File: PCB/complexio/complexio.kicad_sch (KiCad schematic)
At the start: 22 parts, among them J2 Conn_01x21_Pin, J3 USB_C_Receptacle_USB2.0_16P, SW1 SW_SPDT, U2 TB6612FNG, U21 AT24CM01, U22 STM32F303RBT6, U3 TB6612FNG

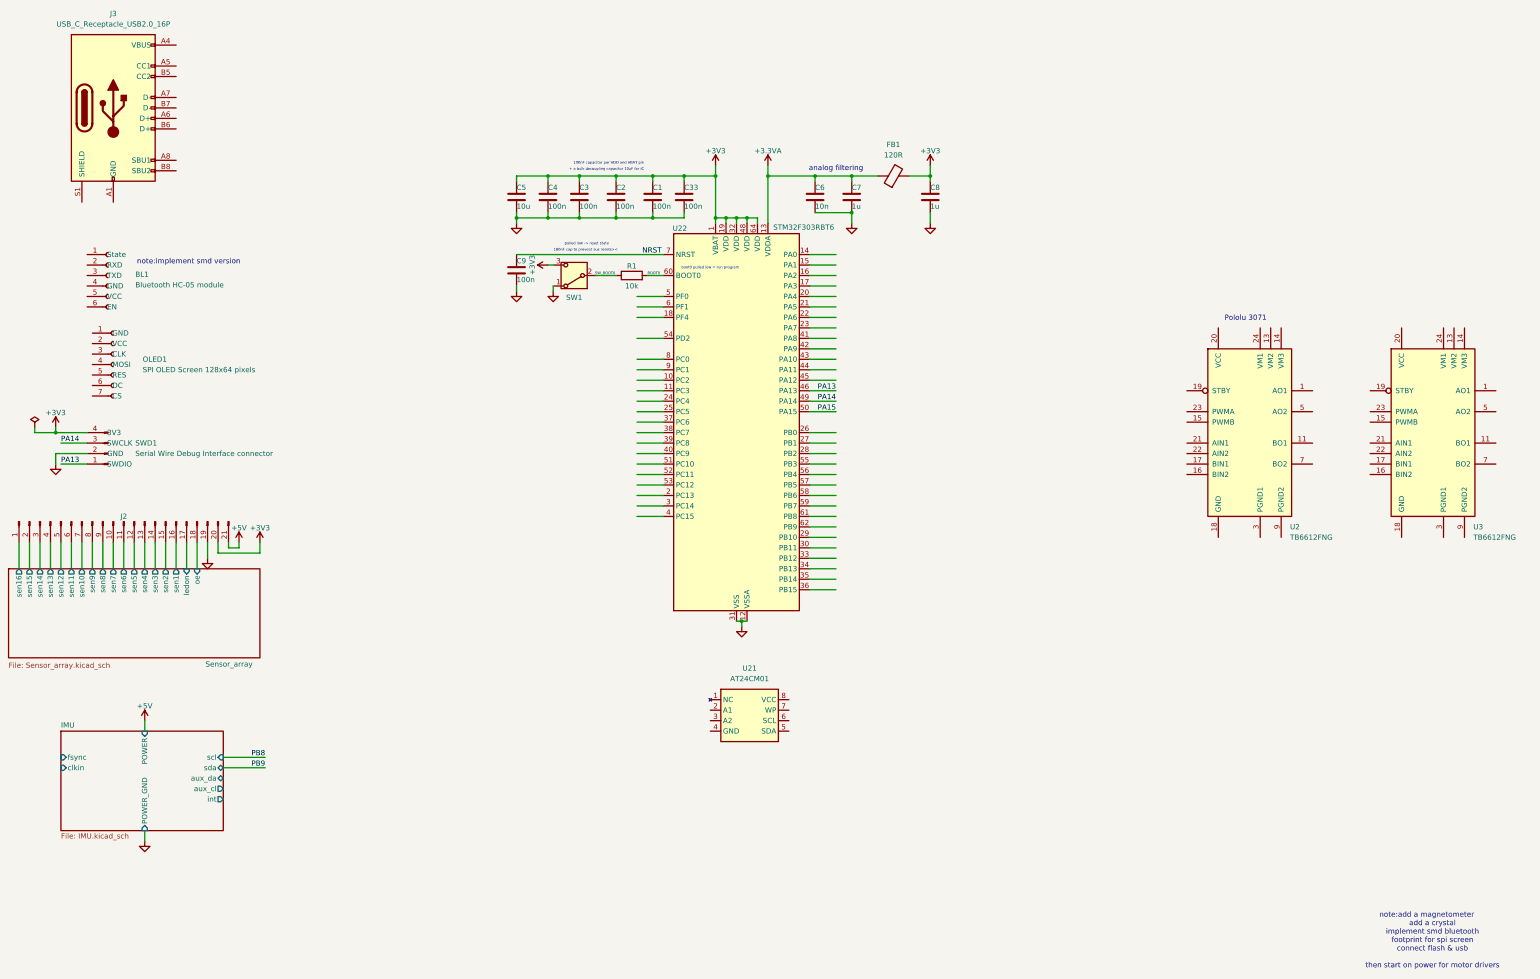
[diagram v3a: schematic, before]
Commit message: Advanced with schem & resolved main power problem
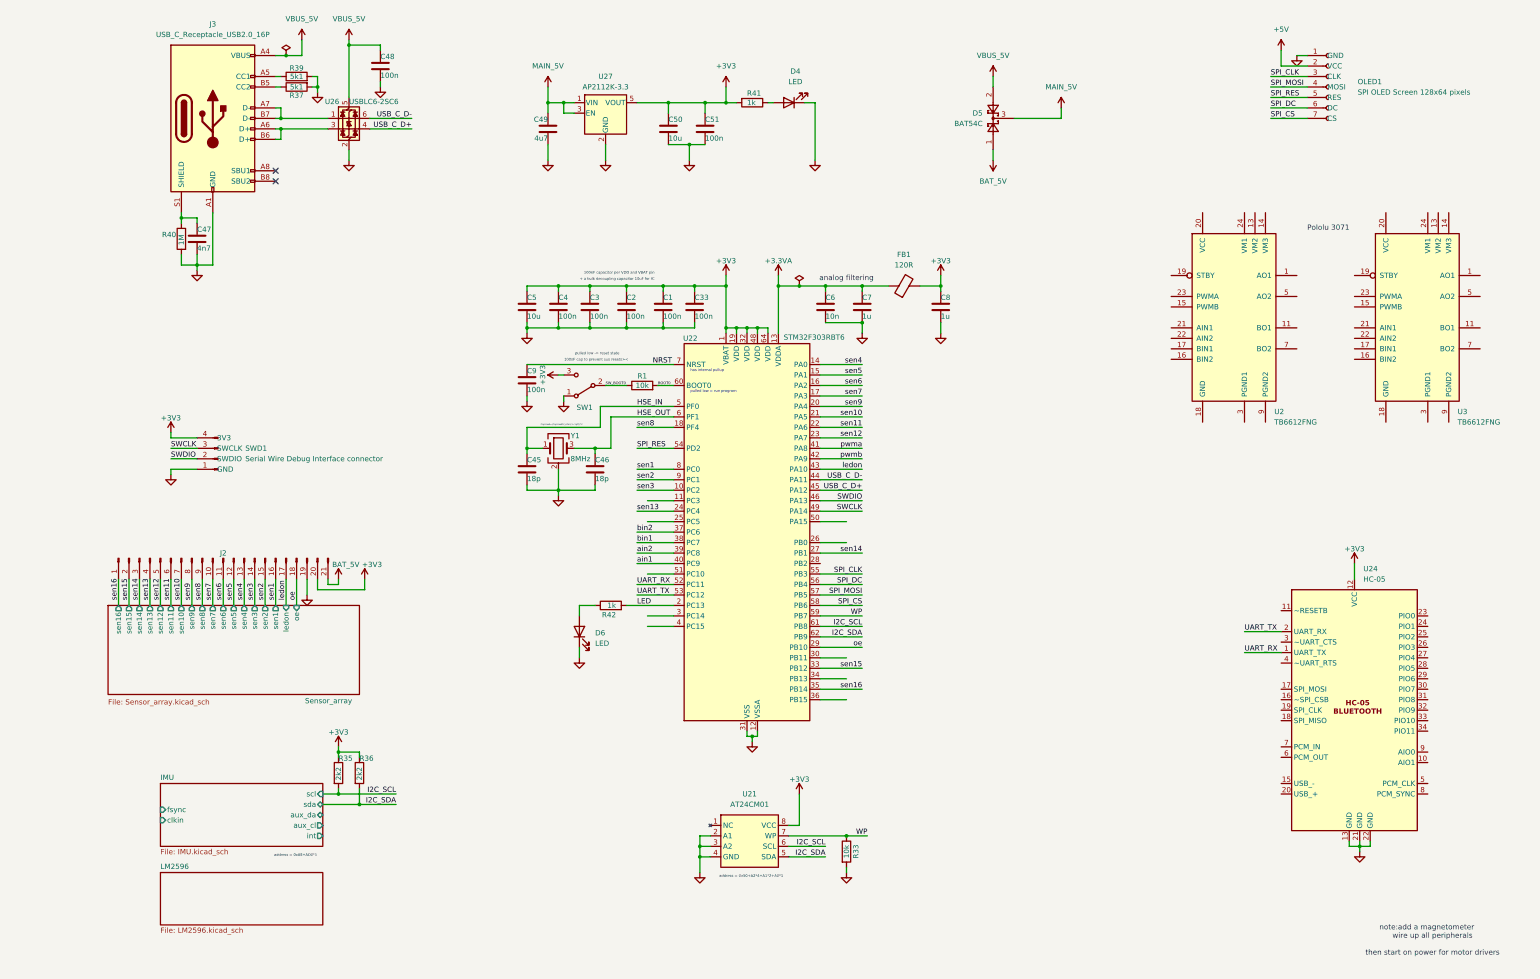
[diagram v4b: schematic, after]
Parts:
- removed BL1: Bluetooth HC-05 module, Connector_PinSocket_2.54mm:PinSocket_1x07_P2.54mm_Horizontal, symbol Connector:Conn_01x06_Socket
- added C45, C46: 18p, Capacitor_SMD:C_0402_1005Metric, symbol Device:C
- added C47: 4n7, Capacitor_SMD:C_1206_3216Metric, symbol Device:C
- added C48, C51: 100n, Capacitor_SMD:C_0402_1005Metric, symbol Device:C
- added C49: 4u7, Capacitor_SMD:C_0603_1608Metric, symbol Device:C
- added C50: 10u, Capacitor_SMD:C_0603_1608Metric, symbol Device:C
- added D4, D6: LED, LED_SMD:LED_0201_0603Metric, symbol Device:LED
- added D5: BAT54C, Package_TO_SOT_SMD:SOT-23, symbol Diode:BAT54C
- added R33: 10k, Resistor_SMD:R_0402_1005Metric, symbol Device:R
- added R35, R36: 2k2, Resistor_SMD:R_0603_1608Metric, symbol Device:R
- added R37, R39: 5k1, Resistor_SMD:R_0603_1608Metric, symbol Device:R
- added R40: 1M, Resistor_SMD:R_1206_3216Metric, symbol Device:R
- added R41, R42: 1k, Resistor_SMD:R_1206_3216Metric, symbol Device:R
- added U24: HC-05, HC-05:HC-05_SMD, symbol HC-05:HC-05
- added U26: USBLC6-2SC6, Package_TO_SOT_SMD:SOT-23-6, symbol Power_Protection:USBLC6-2SC6
- added U27: AP2112K-3.3, Package_TO_SOT_SMD:SOT-23-5, symbol Regulator_Linear:AP2112K-3.3
- added Y1: 8MHz, Crystal:Crystal_SMD_3225-4Pin_3.2x2.5mm, symbol Device:Crystal_GND24
- OLED1: footprint Connector_PinSocket_2.54mm:PinSocket_1x07_P2.54mm_Vertical -> SSD1306_SPI:SSD1306_SPI
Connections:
- net Sensor_array/ledon is gone; now on net ledon: J2.17 (Pin_17)
- net Sensor_array/oe is gone; now on net oe: J2.18 (Pin_18)
- net Sensor_array/sen1 is gone; now on net sen1: J2.16 (Pin_16)
- net Sensor_array/sen10 is gone; now on net sen10: J2.7 (Pin_7)
- net Sensor_array/sen11 is gone; now on net sen11: J2.6 (Pin_6)
- net Sensor_array/sen12 is gone; now on net sen12: J2.5 (Pin_5)
- net Sensor_array/sen13 is gone; now on net sen13: J2.4 (Pin_4)
- net Sensor_array/sen14 is gone; now on net sen14: J2.3 (Pin_3)
- net Sensor_array/sen15 is gone; now on net sen15: J2.2 (Pin_2)
- net Sensor_array/sen16 is gone; now on net sen16: J2.1 (Pin_1)
- net Sensor_array/sen2 is gone; now on net sen2: J2.15 (Pin_15)
- net Sensor_array/sen3 is gone; now on net sen3: J2.14 (Pin_14)
- net Sensor_array/sen4 is gone; now on net sen4: J2.13 (Pin_13)
- net Sensor_array/sen5 is gone; now on net sen5: J2.12 (Pin_12)
- net Sensor_array/sen6 is gone; now on net sen6: J2.11 (Pin_11)
- net Sensor_array/sen7 is gone; now on net sen7: J2.10 (Pin_10)
- net Sensor_array/sen8 is gone; now on net sen8: J2.9 (Pin_9)
- net Sensor_array/sen9 is gone; now on net sen9: J2.8 (Pin_8)
- net +3V3: now also U21.8 (VCC), C50.1, C51.1, R35.1, R36.1, R41.2, U24.12 (VCC), U27.5 (VOUT)
- net +5V: now also OLED1.2 (VCC); no longer J2.21 (Pin_21)
- net GND: now also J3.A1 (GND), J3.A12 (GND), J3.B1 (GND), J3.B12 (GND), OLED1.1 (GND), SWD1.1 (GND), U21.2 (A1), U21.3 (A2), U21.4 (GND), C45.2, C46.2, C47.2, C48.2, C49.2, C50.2, C51.2, D4.1 (K), D6.1 (K), R33.2, R37.2, R39.2, R40.2, U24.13 (GND), U24.21 (GND), U24.22 (GND), U26.2 (GND), U27.2 (GND), Y1.2 (G), Y1.4 (G); no longer SWD1.2 (GND)
- net SPI_CLK: now reaches OLED1.3 (CLK)
- net SPI_CLK: now also U22.55 (PB3)
- net SPI_MOSI: now reaches OLED1.4 (MOSI)
- net SPI_MOSI: now also U22.57 (PB5)
- net SPI_RES: now reaches OLED1.5 (RES)
- net SPI_RES: now also U22.54 (PD2)
- net SPI_DC: now reaches OLED1.6 (DC)
- net SPI_DC: now also U22.56 (PB4)
- net SPI_CS: now reaches OLED1.7 (CS)
- net SPI_CS: now also U22.58 (PB6)
- net I2C_SDA: now reaches U21.5 (SDA)
- net I2C_SDA: now also U22.62 (PB9), R36.2
- net I2C_SCL: now reaches U21.6 (SCL)
- net I2C_SCL: now also U22.61 (PB8), R35.2
- net WP: now reaches U21.7 (WP)
- net WP: now also U22.59 (PB7), R33.1
- net VBUS_5V: now reaches J3.A4 (VBUS), J3.A9 (VBUS), J3.B4 (VBUS), J3.B9 (VBUS)
- net VBUS_5V: now also C48.1, D5.2, U26.5 (VBUS)
- net at J3.A5 (CC1): now also R39.1
- net at J3.A6 (D+): now also J3.B6 (D+), U26.3 (I/O2)
- net at J3.A7 (D-): now also J3.B7 (D-), U26.1 (I/O1)
- net at J3.B5 (CC2): now also R37.1
- net at J3.S1 (SHIELD): now also C47.1, R40.1
- net sen3: now reaches U22.10 (PC2)
- net sen4: now reaches U22.14 (PA0)
- net sen5: now reaches U22.15 (PA1)
- net sen6: now reaches U22.16 (PA2)
- net sen7: now reaches U22.17 (PA3)
- net sen8: now reaches U22.18 (PF4)
- net LED: now reaches U22.2 (PC13)
- net LED: now also R42.2
- net sen9: now reaches U22.20 (PA4)
- net sen10: now reaches U22.21 (PA5)
- net sen11: now reaches U22.22 (PA6)
- net sen12: now reaches U22.23 (PA7)
- net sen13: now reaches U22.24 (PC4)
- net sen14: now reaches U22.27 (PB1)
- net oe: now reaches U22.29 (PB10)
- net sen15: now reaches U22.33 (PB12)
- net sen16: now reaches U22.35 (PB14)
- net bin2: now reaches U22.37 (PC6)
- net bin1: now reaches U22.38 (PC7)
- net ain2: now reaches U22.39 (PC8)
- net ain1: now reaches U22.40 (PC9)
- net pwma: now reaches U22.41 (PA8)
- net pwmb: now reaches U22.42 (PA9)
- net ledon: now reaches U22.43 (PA10)
- net USB_C_D-: now reaches U22.44 (PA11)
- net USB_C_D-: now also U26.6 (I/O1)
- net USB_C_D+: now reaches U22.45 (PA12)
- net USB_C_D+: now also U26.4 (I/O2)
- net HSE_IN: now reaches U22.5 (PF0)
- net HSE_IN: now also C45.1, Y1.1
- net UART_RX: now reaches U22.52 (PC11)
- net UART_RX: now also U24.1 (UART_TX)
- net UART_TX: now reaches U22.53 (PC12)
- net UART_TX: now also U24.2 (UART_RX)
- net HSE_OUT: now reaches U22.6 (PF1)
- net HSE_OUT: now also C46.1, Y1.3
- net sen1: now reaches U22.8 (PC0)
- net sen2: now reaches U22.9 (PC1)
- net PA13 renamed SWDIO
- net SWDIO: now also SWD1.2 (SWDIO); no longer SWD1.1 (SWDIO)
- net PA14 renamed SWCLK
- net PA15: no longer names the net of U22.50 (PA15)
- new net: D4.2 (A), R41.1
- new net: D6.2 (A), R42.1
- new net BAT_5V: D5.1, J2.21 (Pin_21)
- new net MAIN_5V: C49.1, D5.3, U27.1 (VIN), U27.3 (EN)
- no-connect marks 0 -> 2
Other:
- added sheet LM2596 (LM2596.kicad_sch)
- sheet IMU ports: added none; removed POWER, POWER_GND
- note added: "CapLoad=(CapLoadCrystal-(3~5pF))*2"
- note added: "address = 0x50+A2*4+A1*2+A0*1"
- note added: "address = 0x68+AD0*1"
- note added: "has internal pullup"
- note added: "note:add a magnetometer wire up all peripherals then start on power for motor drivers"
- note added: "pulled low = run program"
- note removed: "boot0 pulled low = run program"
- note removed: "note:add a magnetometer add a crystal implement smd bluetooth footprint for spi screen connect flash & usb then start on power for motor drivers"
- note removed: "note:implement smd version"
- moved on the sheet: C1, C2, C3, C33, C4, C5, C6, C7, C8, C9, FB1, J2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
